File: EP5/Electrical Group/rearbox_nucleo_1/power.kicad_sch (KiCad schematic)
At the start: 72 parts, among them IC1 LM22676MRX-ADJ_NOPB, IC6 MCP6C04T-100E_CHY, J6 24V, J6 24V test, J6 3V3 test, J6 5V external, J6 5V test, J6 5Vout, U2 LP2985-3.3, U3 LM7805_TO220

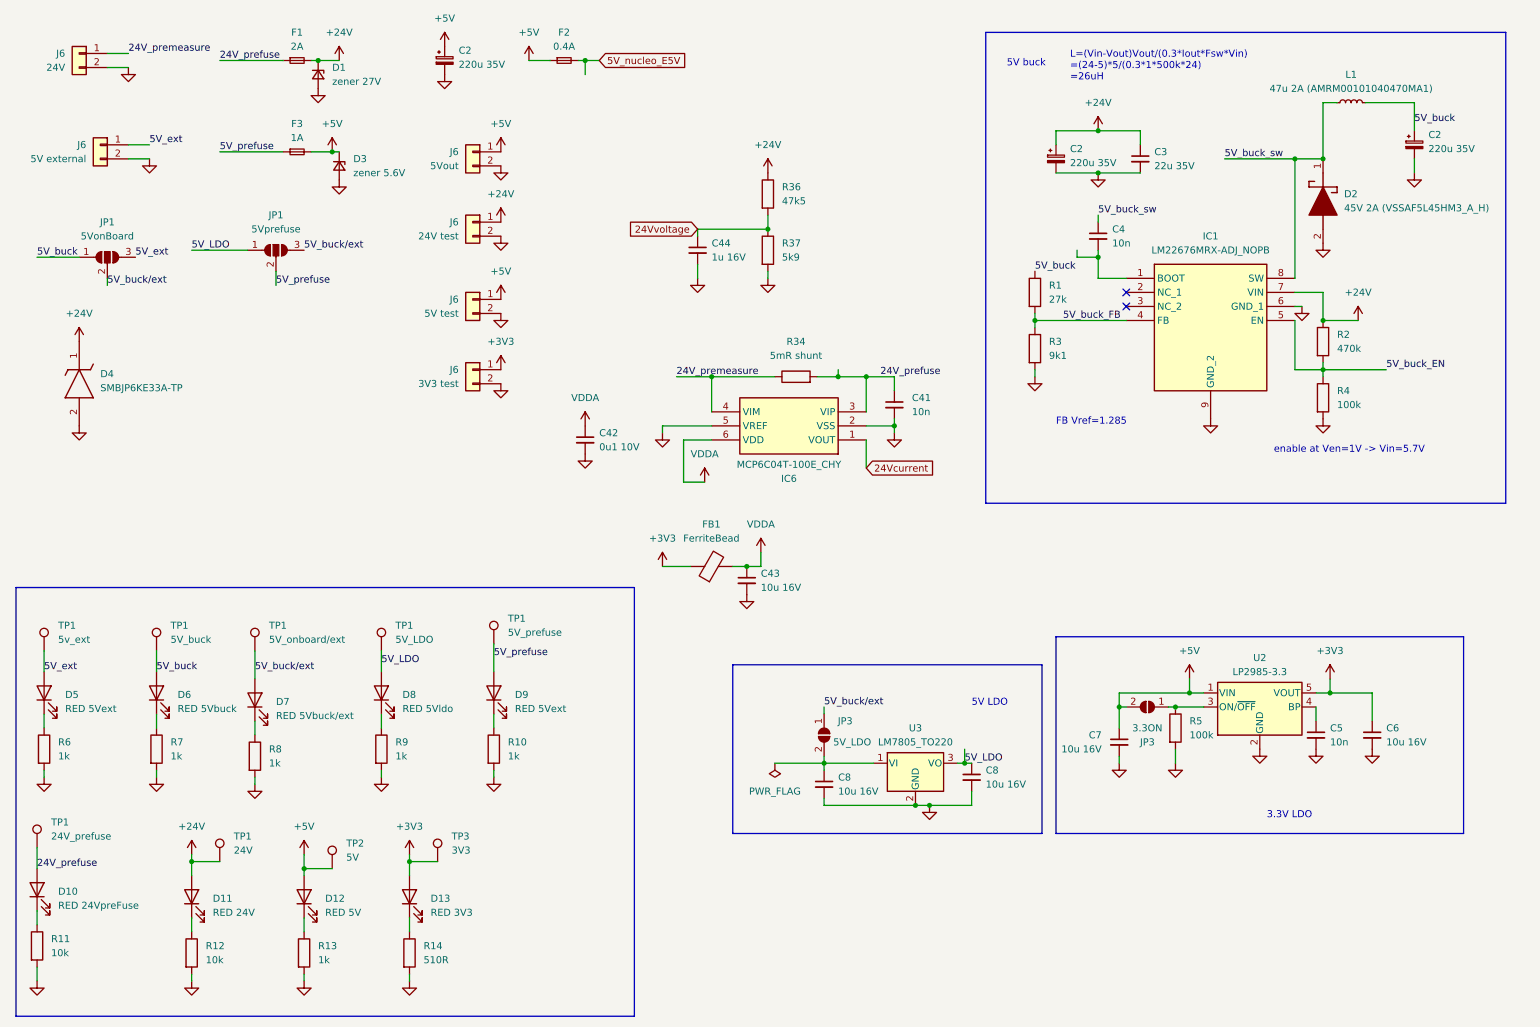
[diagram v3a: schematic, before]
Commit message: update rearbox nucleo hat for kicad 8
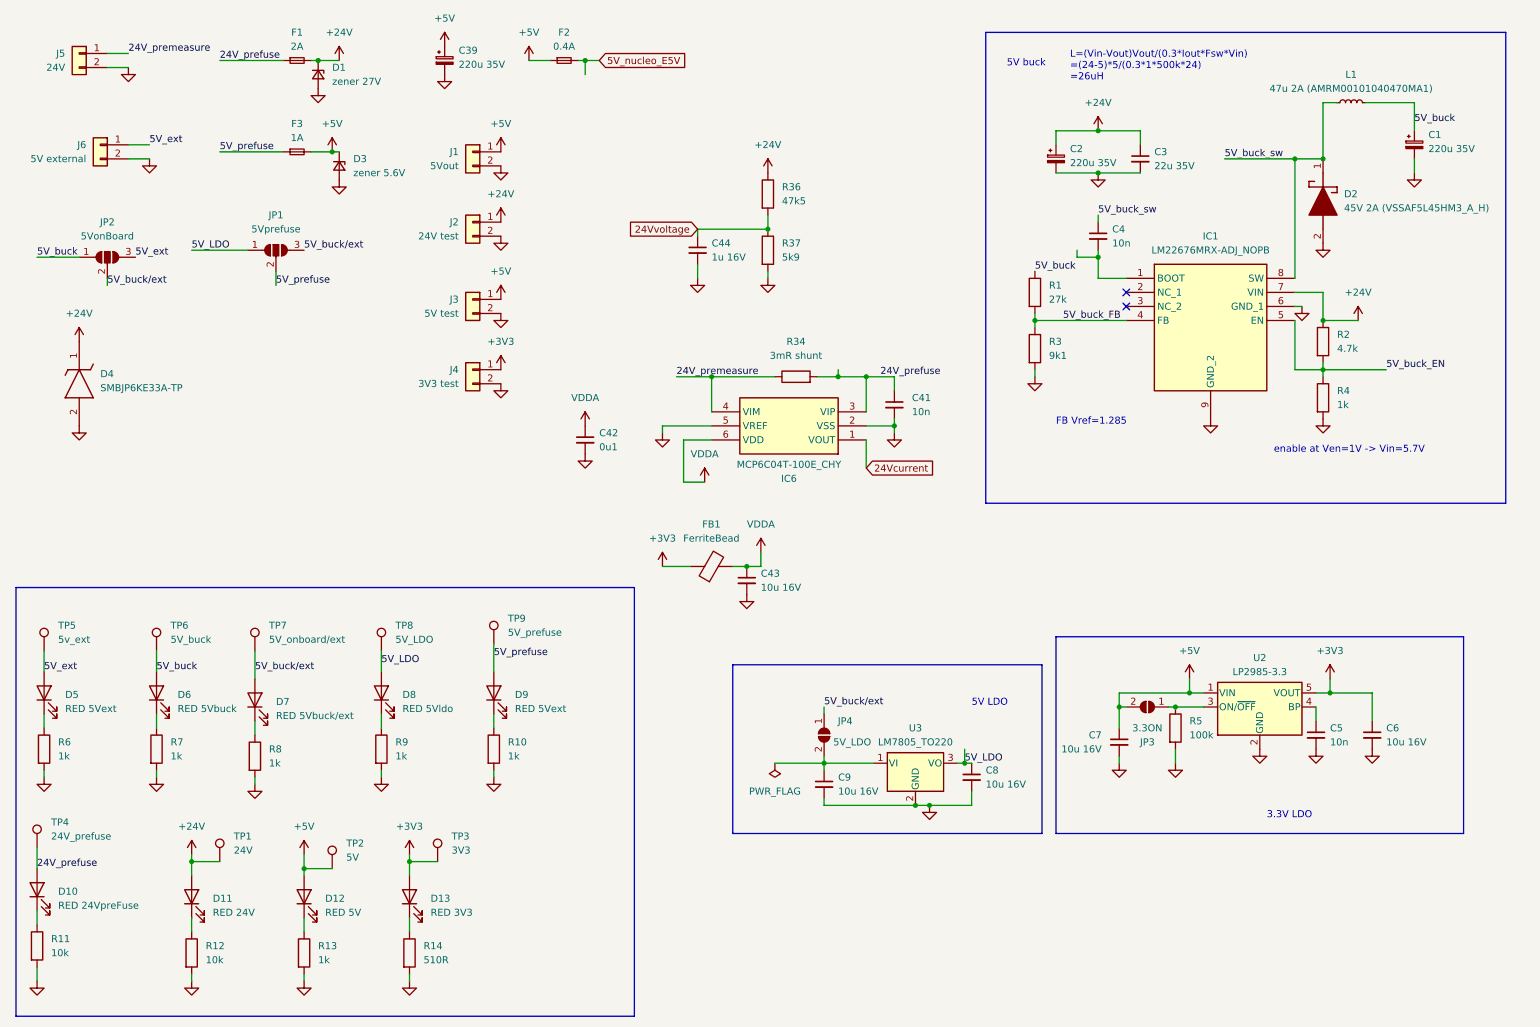
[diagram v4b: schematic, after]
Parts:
- C41, C44: footprint Capacitor_SMD:C_0805_2012Metric -> Capacitor_SMD:C_0603_1608Metric
- C42: value 0u1 10V -> 0u1; footprint Capacitor_SMD:C_0805_2012Metric -> Capacitor_SMD:C_0603_1608Metric
- R2: value 470k -> 4.7k
- R34: value 5mR shunt -> 3mR shunt
- R4: value 100k -> 1k
- renumbered C2 to C1, C2 to C39, C8 to C9, J6 to J1, J6 to J2, J6 to J3, J6 to J4, J6 to J5, JP1 to JP2, JP3 to JP4, TP1 to TP4, TP1 to TP5, TP1 to TP6, TP1 to TP7, TP1 to TP8, TP1 to TP9

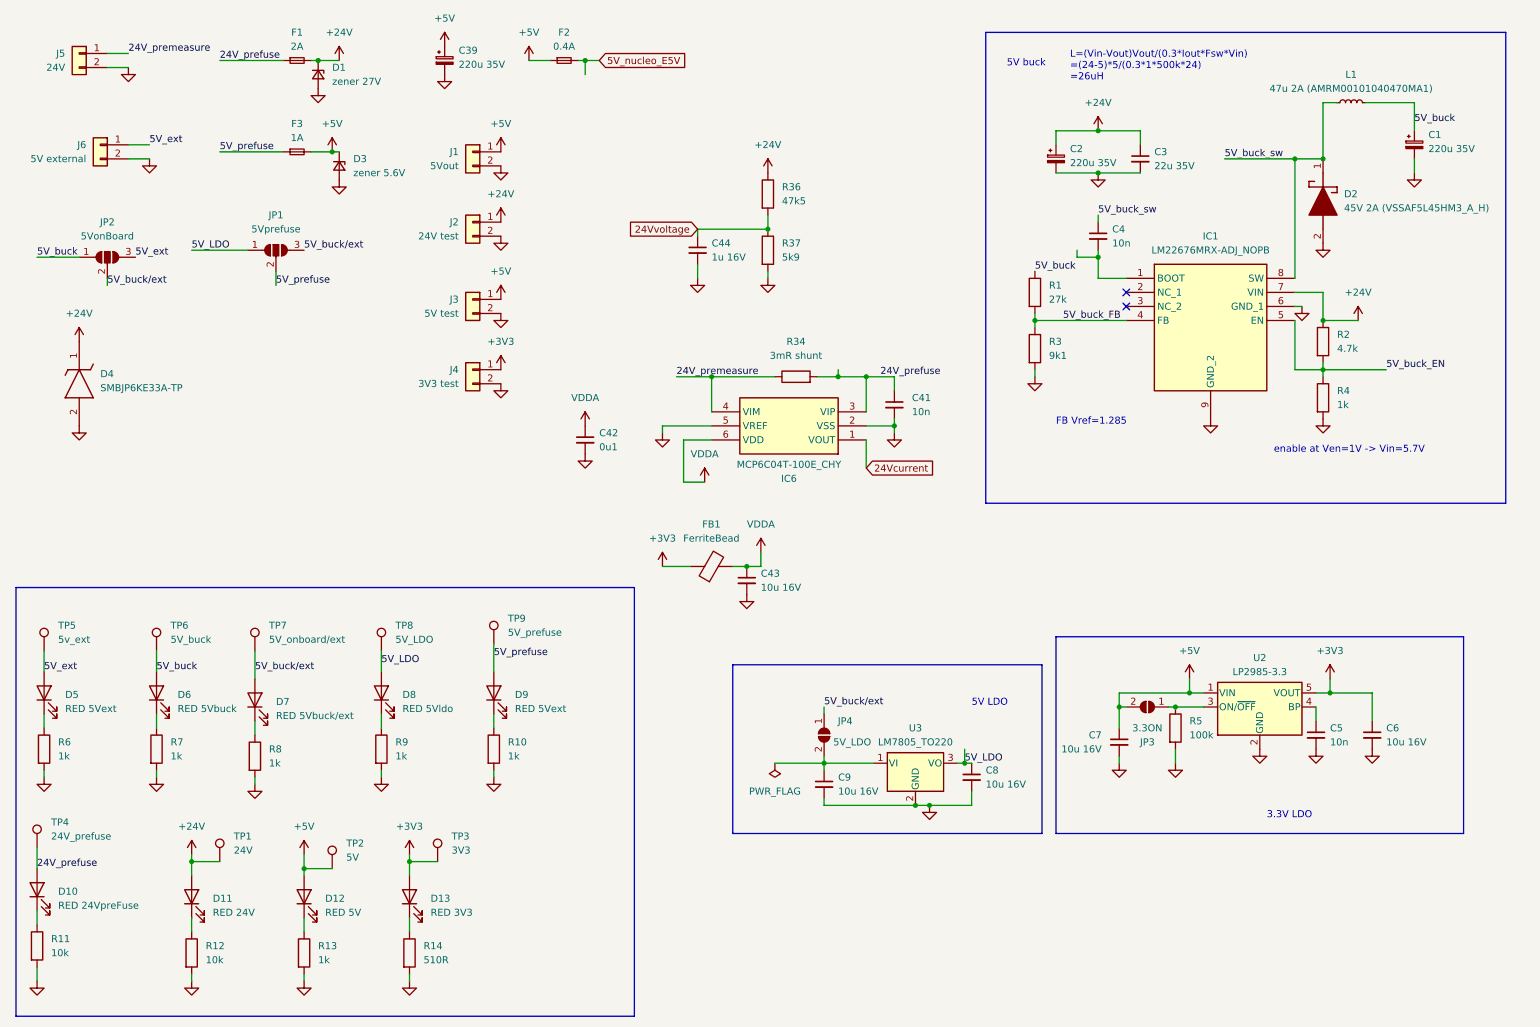
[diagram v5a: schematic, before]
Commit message: update rearbox_nucleo_1 to V3.2 in EP5
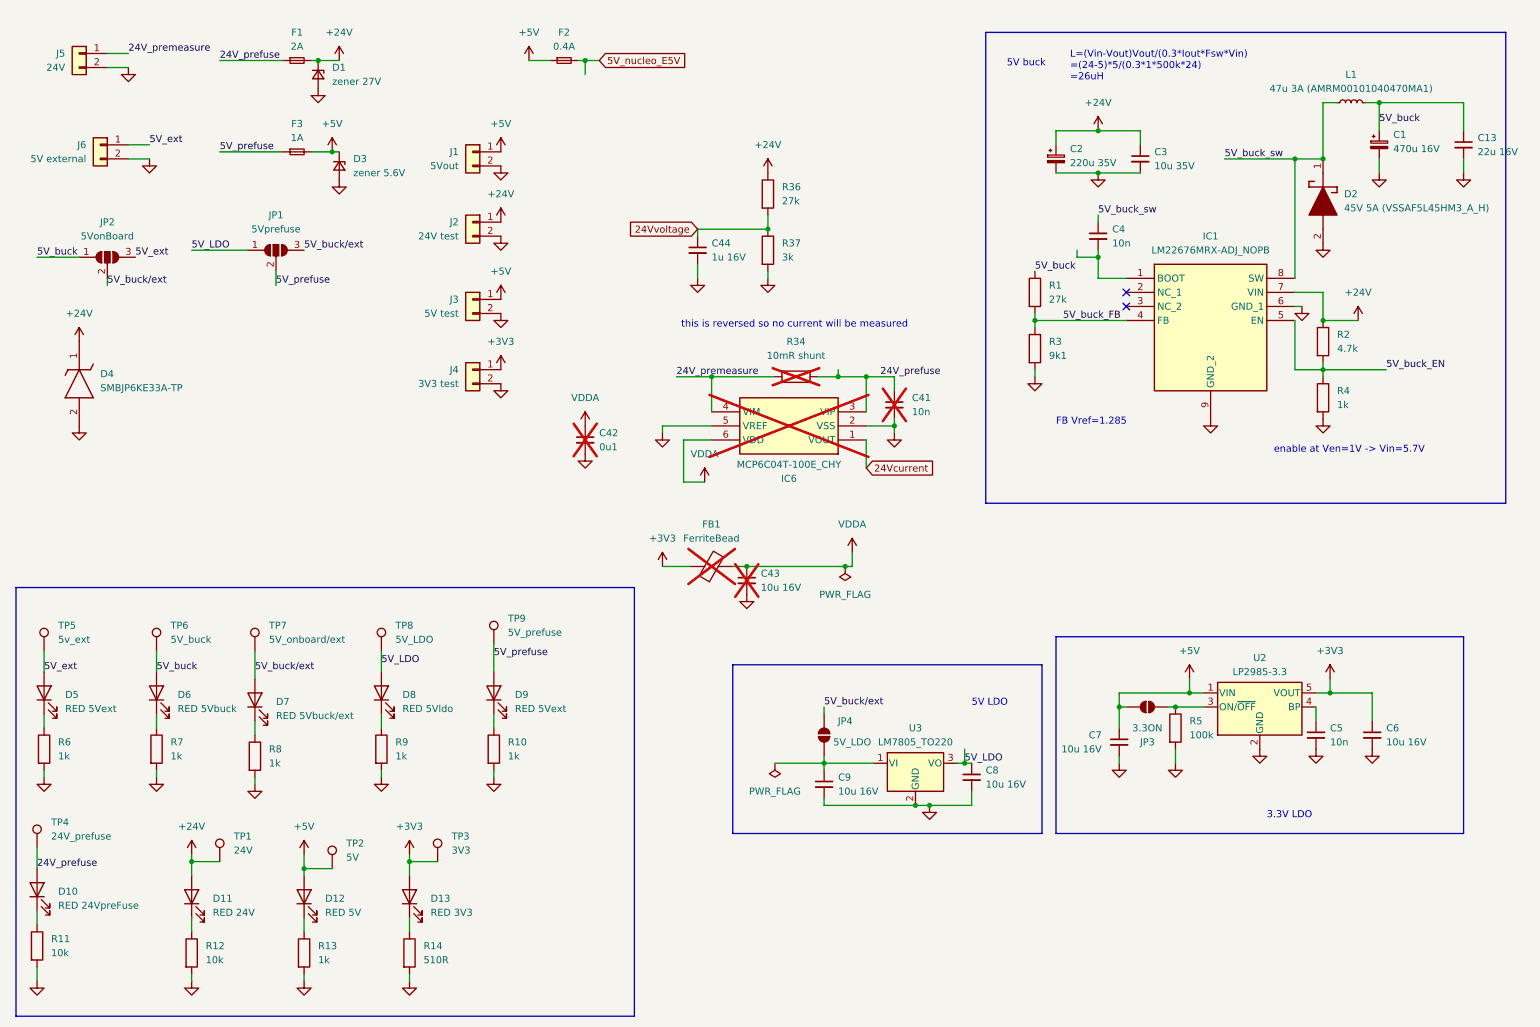
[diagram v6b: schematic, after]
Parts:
- removed C39: 220u 35V, Capacitor_THT:CP_Radial_D8.0mm_P3.80mm, symbol Device:C_Polarized_Small
- added C13: 22u 16V, Capacitor_SMD:C_1206_3216Metric, symbol Device:C_Small
- C1: value 220u 35V -> 470u 16V
- C3: value 22u 35V -> 10u 35V
- C41, C42, C43, FB1, IC6: now not fitted
- D1: footprint Diode_SMD:D_MiniMELF -> PCM_Diode_THT_AKL:D_DO-35_SOD27_P3.81mm_Vertical_KathodeUp_Zener
- D2: value 45V 2A (VSSAF5L45HM3_A_H) -> 45V 5A (VSSAF5L45HM3_A_H)
- L1: value 47u 2A (AMRM00101040470MA1) -> 47u 3A (AMRM00101040470MA1)
- R34: value 3mR shunt -> 10mR shunt; now not fitted
- R36: value 47k5 -> 27k
- R37: value 5k9 -> 3k
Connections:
- net 5V_buck: now also C13.1
- net GND: now also C13.2
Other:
- note added: "this is reversed so no current will be measured"
- moved on the sheet: C1
